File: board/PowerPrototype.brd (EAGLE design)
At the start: 70.8 x 50.8 mm, 21 parts, among them IC1 7805T, Q1 IRF4905, T2 BT138-H

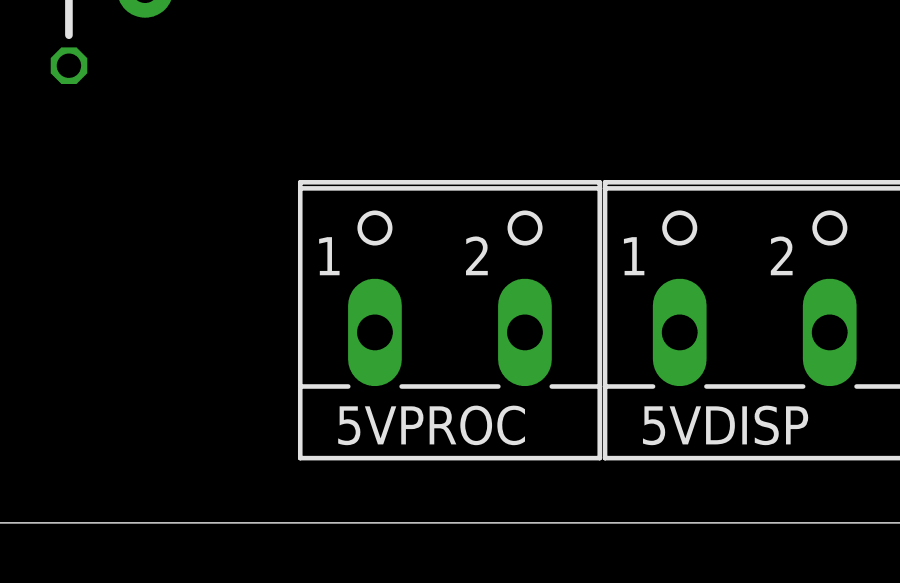
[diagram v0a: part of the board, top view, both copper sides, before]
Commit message: Initial pass at a PCB and added clock code
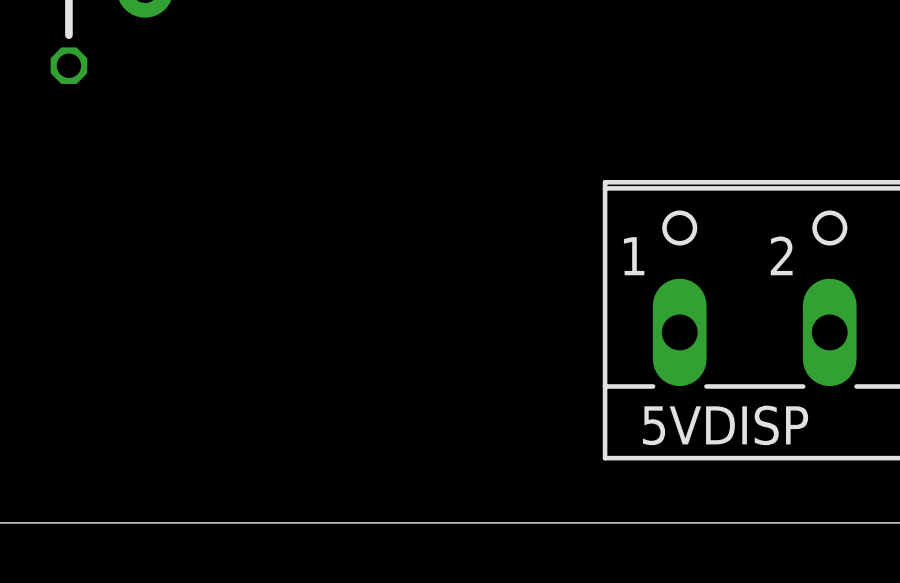
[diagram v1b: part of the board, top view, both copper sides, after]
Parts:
- removed 5VPROC: (no value), con-wago-500:W237-102
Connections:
- net GND: no longer 5VPROC.2
- net N$9: no longer 5VPROC.1
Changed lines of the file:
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@@
 <attribute name="OC_FARNELL" value="unknown" x="6.35" y="50.8" size="1.778" layer="27" rot="R270" display="off"/>
-</element>
-<element name="5VPROC" library="con-wago-500" package="W237-102" value="" x="43.18" y="17.78">
-<attribute name="OC_NEWARK" value="70K9898" x="33.02" y="33.02" size="1.778" layer="27" display="off"/>
-<attribute name="MPN" value="237-102" x="33.02" y="33.02" size="1.778" layer="27" display="off"/>
-<attribute name="MF" value="" x="33.02" y="33.02" size="1.778" layer="27" display="off"/>
-<attribute name="OC_FARNELL" value="unknown" x="33.02" y="33.02" size="1.778" layer="27" display="off"/>
 </element>
 <element name="24VOUT" library="con-wago-500" package="W237-102" value="" x="6.35" y="40.64" rot="R270">
@@
 <contactref element="24VIN" pad="2"/>
 <contactref element="IC1" pad="2"/>
-<contactref element="5VPROC" pad="2"/>
 <contactref element="5VDISP" pad="2"/>
 <contactref element="5VPOT" pad="2"/>
@@
 <wire x1="68.58" y1="31.75" x2="66.04" y2="32.98" width="0" layer="19" extent="1-1"/>
 <wire x1="60.96" y1="33.02" x2="66.04" y2="32.98" width="0" layer="19" extent="1-1"/>
-<wire x1="66" y1="16.51" x2="60.96" y2="33.02" width="0" layer="19" extent="1-1"/>
+<wire x1="66" y1="16.51" x2="68.58" y2="31.75" width="0" layer="19" extent="1-1"/>
 <wire x1="55.84" y1="16.51" x2="66" y2="16.51" width="0" layer="19" extent="1-1"/>
-<wire x1="45.68" y1="16.51" x2="55.84" y2="16.51" width="0" layer="19" extent="1-1"/>
-<wire x1="40.64" y1="33.02" x2="55.84" y2="16.51" width="0" layer="19" extent="1-1"/>
+<wire x1="40.64" y1="33.02" x2="60.96" y2="33.02" width="0" layer="19" extent="1-1"/>
 <wire x1="33.02" y1="35.56" x2="40.64" y2="33.02" width="0" layer="19" extent="1-1"/>
 <wire x1="22.86" y1="43.14" x2="33.02" y2="35.56" width="0" layer="19" extent="1-1"/>
@@
 <contactref element="5VPOT" pad="1"/>
 <contactref element="5VDISP" pad="1"/>
-<contactref element="5VPROC" pad="1"/>
 <contactref element="IC1" pad="3"/>
 <contactref element="C2" pad="+"/>
@@
 <wire x1="66.04" y1="27.98" x2="68.58" y2="29.21" width="0" layer="19" extent="1-1"/>
 <wire x1="60.96" y1="30.48" x2="66.04" y2="27.98" width="0" layer="19" extent="1-1"/>
-<wire x1="61" y1="16.51" x2="60.96" y2="30.48" width="0" layer="19" extent="1-1"/>
+<wire x1="61" y1="16.51" x2="66.04" y2="27.98" width="0" layer="19" extent="1-1"/>
 <wire x1="50.84" y1="16.51" x2="61" y2="16.51" width="0" layer="19" extent="1-1"/>
-<wire x1="40.68" y1="16.51" x2="50.84" y2="16.51" width="0" layer="19" extent="1-1"/>
 </signal>
 <signal name="N$1">
